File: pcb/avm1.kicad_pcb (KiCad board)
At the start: 2 copper layers, 100.6 x 100 mm, 81 parts, among them J1 Video_Output, J10 Front_Conn_1, J11 Front_Conn_3, J12 Back_Conn_2, J13 Back_Conn_3, J14 Back_Conn_1, J15 Front_Conn_4, J16 Back_Conn_4, J17 VIN, J2 Jack_X_CV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

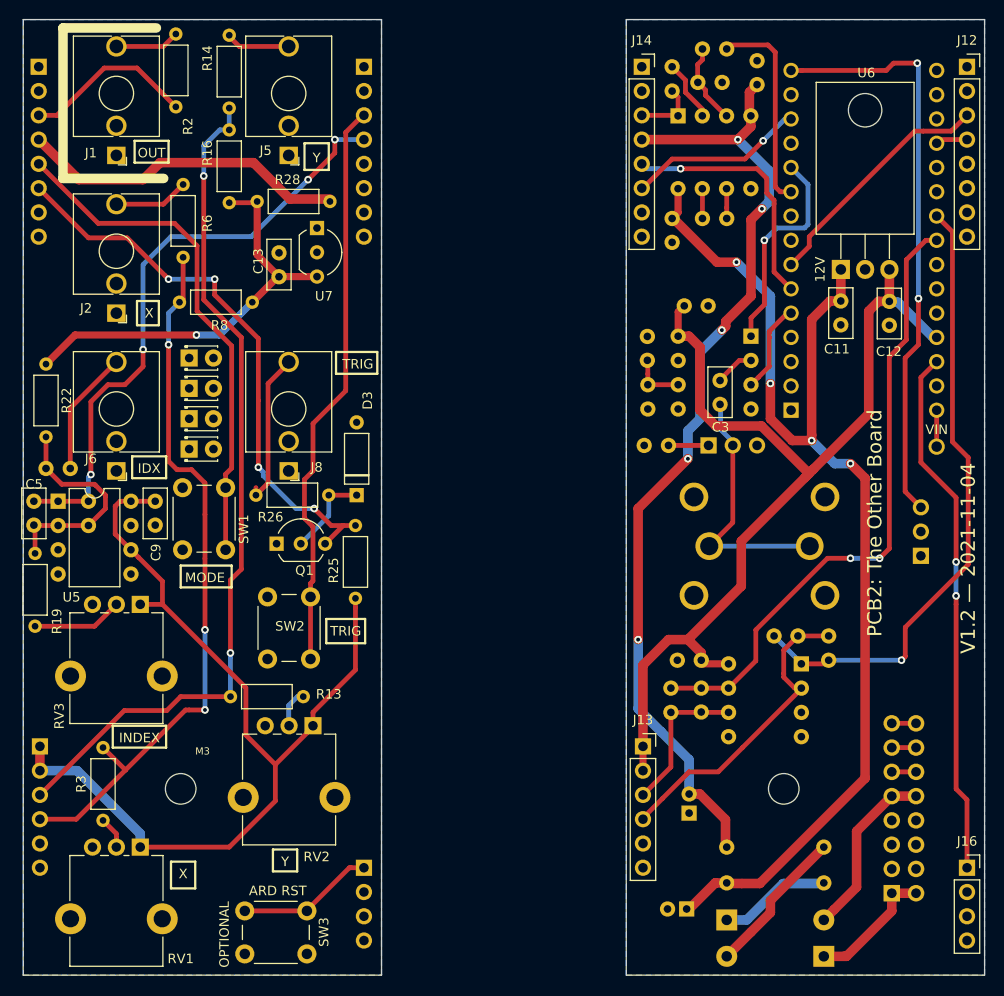
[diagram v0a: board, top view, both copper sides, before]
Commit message: Added SMD LM1881 footprint, moved a few things around
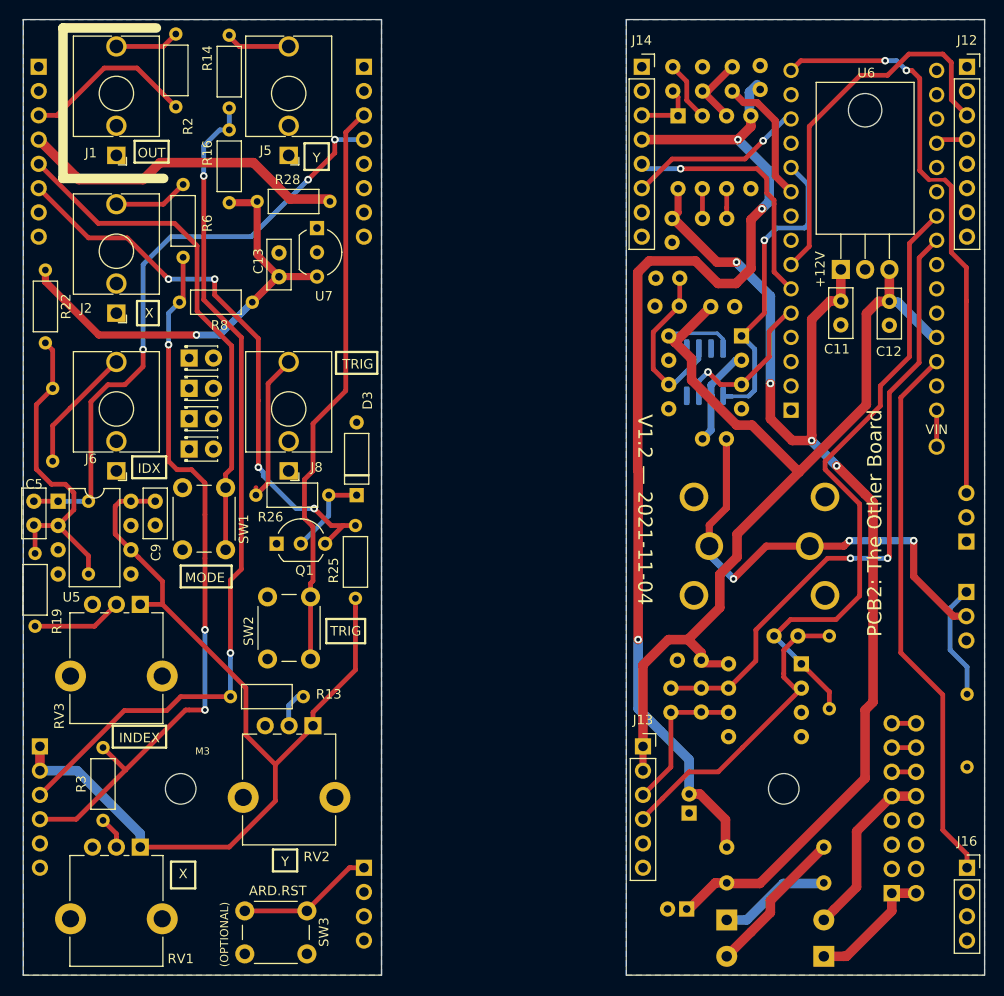
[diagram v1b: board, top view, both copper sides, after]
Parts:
- added U4: LM1881, Package_SO:SOIC-8_3.9x4.9mm_P1.27mm, B.Cu at (109.7, 70.2)
- C3: moved to B.Cu
- H1: value H1 -> MountingHole
- H2: value H2 -> MountingHole
- R10, R20, R21, R7: footprint Resistor_THT:R_Axial_DIN0207_L6.3mm_D2.5mm_P2.54mm_Vertical -> jwm_kicad_footprints_misc:R_Axial_P7.62mm_Horizontal_LZX
- moved R10 47.7 mm to (137.2, 111.5), turned to 90 degrees
- moved JP2 31.0 mm to (137.1, 93.2), turned to 180 degrees
- moved R11 10.8 mm to (104.5, 63.3), turned to 0 degrees
- moved R22 9.84 mm to (40.7, 59.5)
- moved C4 9.24 mm to (107.1, 60.4), turned to 180 degrees
- moved R20 8.41 mm to (41.5, 71.9), turned to 270 degrees
- moved R7 5.08 mm to (122.7, 105.4)
- moved JP1 4.99 mm to (137.1, 87.9)
- moved C3 3.67 mm to (112.0, 77.2), turned to 180 degrees
- moved R1 3.63 mm to (112.6, 38.2), turned to 270 degrees
- moved C8 2.78 mm to (110.3, 63.3)
- moved R4 2.62 mm to (109.5, 38.2), turned to 270 degrees
- moved U3 0.99 mm to (113.6, 66.4)
- moved C10 0.60 mm to (115.5, 38.1)
- moved R5 0.07 mm to (106.4, 38.2)
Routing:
- net Net-(C3-Pad1): track 27.0 -> 47.9 mm, vias 0 -> 3
- net /TRIGGER_SWITCH_BACK: track 25.5 -> 39.8 mm
- net Net-(C4-Pad1): track 5.72 -> 18.3 mm
- net Net-(C5-Pad2): track 23.3 -> 35.1 mm
- net /C_SYNC: track 22.6 -> 32.8 mm
- net -12V: track 102.4 -> 111.1 mm, vias 5 -> 3
- net Net-(JP2-Pad1): track 4.19 -> 12.1 mm
- net /VIDEO: track 21.5 -> 13.9 mm
- net /V_SYNC: track 9.45 -> 16.8 mm, vias 0 -> 1
- net +5V: track 104.3 -> 110.6 mm
- net Net-(C3-Pad2): track 4.11 -> 10.3 mm
- net -5V: track 44.1 -> 46.4 mm
- net /RESET_SWITCH_BACK: track 55.8 -> 57.4 mm, vias 2 -> 0
- net /X_CV: track 65.4 -> 66.8 mm, vias 1 -> 0
- net GND2: track 0.00 -> 1.07 mm
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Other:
- board text added: "(OPTIONAL)"
- board text added: "+12V"
- board text added: "ARD.RST"
- board text added: "FORMAT SETTING"
- board text added: "SYNC SETTING"
- board text removed: "12V"
- board text removed: "ARD RST"
- board text removed: "FORMAT"
- board text removed: "OPTIONAL"

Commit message: Do a bunch of improvements
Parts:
- removed REF** (x4): LED_D1.8mm_W3.3mm_H2.4mm, LED_THT:LED_D1.8mm_W3.3mm_H2.4mm
- removed SW3: Button_Arduino_Reset, Button_Switch_THT:SW_PUSH_6mm_H9.5mm
- A1: footprint Module:Arduino_Nano -> jwm_kicad_footprints_misc:Arduino_Nano_WithMFHeadersAnd3DModel
- C14, C15: footprint Capacitor_THT:CP_Radial_D5.0mm_P2.00mm -> jwm_kicad_footprints_misc:CP_Radial_D5.0mm_P2.00mm_BiggerPlusSign
- J1, J2, J5, J6, J8: footprint Connector_Audio:Jack_3.5mm_QingPu_WQP-PJ398SM_Vertical_CircularHoles -> jwm_kicad_footprints_misc:Jack_3.5mm_QingPu_WQP-PJ398SM_Vertical_CircularHoles_With3DModel
- J9: value Eurorack_Header_LZX -> Eurorack_Header_LZX_NC-5vCvGate
- R20: moved to F.Cu
- U1, U2, U3: footprint Package_DIP:DIP-8_W7.62mm -> jwm_kicad_footprints_misc:DIP-8_W7.62mm_MediumOffsetPads
- U4: footprint Package_SO:SOIC-8_3.9x4.9mm_P1.27mm -> jwm_kicad_footprints_misc:SOIC-8_3.9x4.9mm_P1.27mm_LongPads
- moved C10 0.44 mm to (115.5, 37.7)
- moved R1 0.44 mm to (112.6, 37.8)
- moved R4 0.44 mm to (109.5, 37.8)
- moved R5 0.44 mm to (106.4, 37.8)
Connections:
- A1 pad 28: /RESET_SWITCH_BACK -> Net-(A1-Pad28)
- J15 pad 1: /RESET_SWITCH_FRONT -> GND1
- J16 pad 1: /RESET_SWITCH_BACK -> GND2
- J9 pad 12: Net-(J9-Pad11) -> Net-(J9-Pad12)
- J9 pad 14: Net-(J9-Pad13) -> Net-(J9-Pad14)
- J9 pad 16: Net-(J9-Pad15) -> Net-(J9-Pad16)
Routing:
- net /RESET_SWITCH_BACK: track 57.4 -> 0.00 mm
- net /RESET_SWITCH_FRONT: track 14.3 -> 0.00 mm
- net Net-(J9-Pad11): track 2.67 -> 0.00 mm
- net Net-(J9-Pad15): track 2.54 -> 0.00 mm
- net Net-(J9-Pad13): track 2.54 -> 0.00 mm
- net +5V: track 110.6 -> 109.1 mm
- net /VIDEO: track 13.9 -> 14.8 mm
- net /X_CV_PRE_FRONT: track 75.8 -> 74.9 mm
- net /C_SYNC: track 32.8 -> 33.5 mm
- net Net-(C4-Pad1): track 18.3 -> 18.9 mm
- net /MODE_SWITCH_FRONT: track 53.8 -> 53.3 mm
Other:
- board text added: "AVML"
- board text added: "B"
- board text added: "C"
- board text added: "E"
- board text added: "TODO: Update the version and date when ready!!!!!!!!"
- board text added: "V1.2/3 — YYYY-MM-DD"
- board text removed: "(OPTIONAL)"
- board text removed: "ARD.RST"
- board text removed: "AVM1"
- board text removed: "TODO: Add 3D models for the jacks and arduino!"
- board text removed: "TODO: Replace the DIP LM1881 with a SOIC one! (or a dual format footprint?)"
- board text removed: "V1.2 — 2021-11-04"

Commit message: tweaked some more things
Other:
- board text added: "V1.3 — 2022-10-22"
- board text removed: "V1.2/3 — YYYY-MM-DD"
